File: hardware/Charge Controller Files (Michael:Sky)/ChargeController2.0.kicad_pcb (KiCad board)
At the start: 2 copper layers, 90.2 x 95.9 mm, 90 parts, among them J1 GND_TEST_01x01_Pin, J10 SOL_TEST_01x01_Pin, J13 Conn-1x2, J14 Conn-1x2, J15 Conn-1x2, J17 SCL_MAS_01x01_Pin, J18 SDA_MAS_01x01_Pin, J19 SYS-1x2, J2 SP_01x02_Pin, J3 BATT_TEST_01x01_Pin, J4 3.3V_PULLUP_01x02_Pin, J5 BATT_01x02_Pin, J6 Conn-1x2, J7 Conn-1x2, J8 Conn-1x2, J9 SYS_TEST_01x01_Pin, Q1 SI2318DS-T1-E3, Q10 SI2318DS-T1-E3, Q11 SI2318DS-T1-E3, Q12 SI2318DS-T1-E3, Q2 SI2318DS-T1-E3, Q3 SI2318DS-T1-E3, Q4 SI2318DS-T1-E3, Q5 AONS66614, Q6 AONS66614, Q7 AONS66614, Q8 AONS66614, Q9 SI2318DS-T1-E3, SW1 100SP1T1B1M1QEH, U1 BQ25756ERRVR

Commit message: PCB fixes
Routing changes
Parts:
- moved C17 1.58 mm to (199.0, 107.5)
- moved R_AC2 1.00 mm to (170.5, 105.5)
- moved D7 0.71 mm to (143.0, 51.7), turned to -90 degrees
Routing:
- net Net-(D7-PadC): track 27.7 -> 21.9 mm
- net Net-(Q1-DRAIN): track 56.0 -> 50.8 mm
- net Net-(Q11-DRAIN): track 119.2 -> 115.9 mm
- net /ACOV: track 14.3 -> 13.3 mm
- net /ACUV: track 15.8 -> 14.9 mm
- net GND: track 81.1 -> 80.5 mm

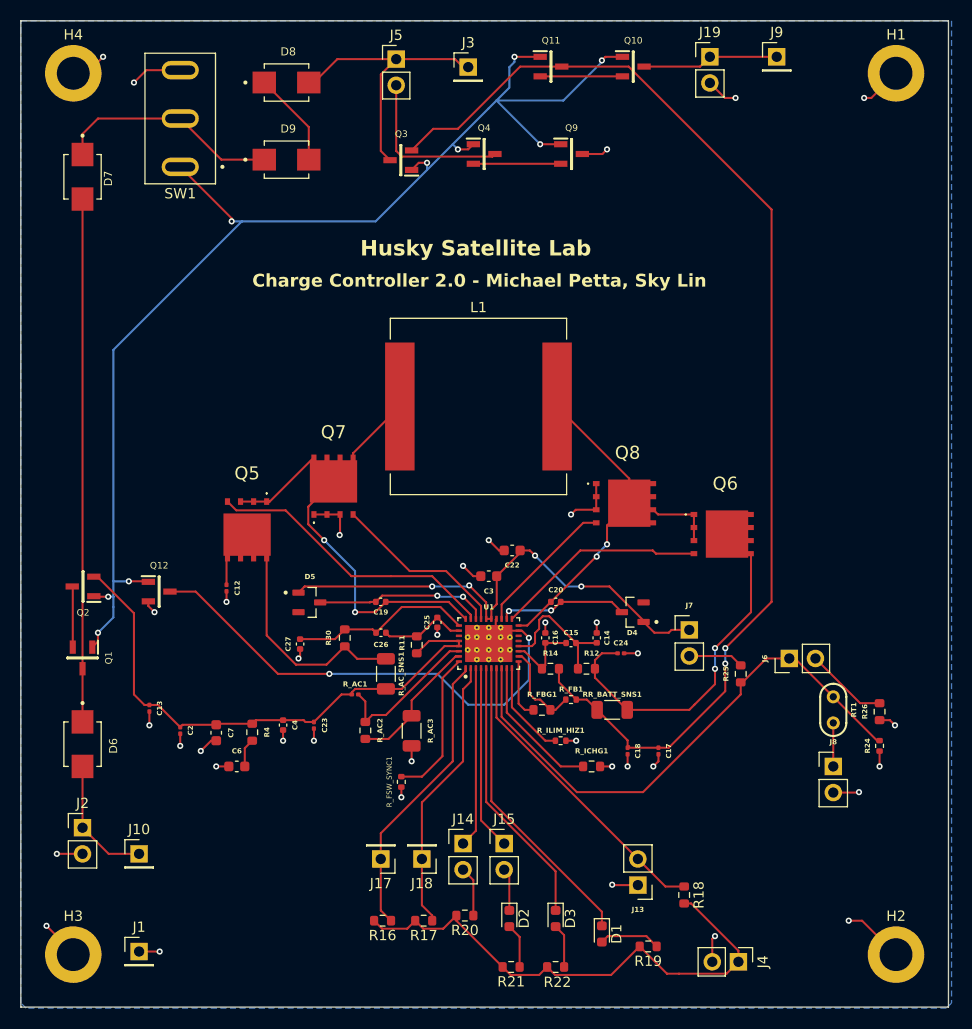
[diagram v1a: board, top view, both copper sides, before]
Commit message: PCB fixes
Changed RAC_3 symbol and footprint, changed Inhibits mosfets to later (better) version.
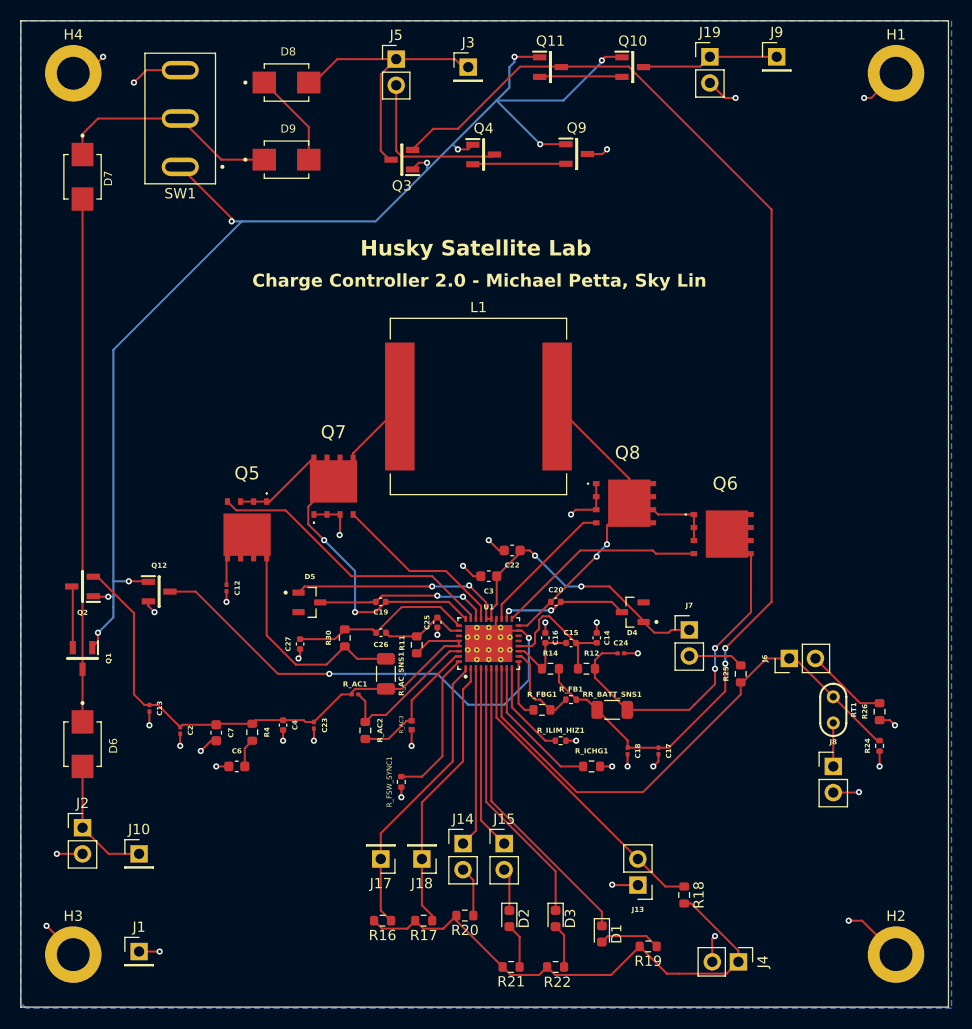
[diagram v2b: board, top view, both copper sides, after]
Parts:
- Q1, Q10, Q11, Q12, Q2, Q3, Q4, Q9: value SI2318DS-T1-E3 -> SI2318CDS-T1-GE3; footprint bmsfootprints:SI2318DS-T1-E3 -> bmsfootprints:SI2318CDS-T1-GE3
- R_AC3: value 53.25 -> RC0402FR-0753K6L; footprint Resistor_SMD:R_1206_3216Metric -> bmsfootprints:RC0402FR-0753K6L
- moved R_AC3 0.54 mm to (175.0, 105.0)
- moved Q9 0.50 mm to (191.1, 49.5)
- moved Q3 0.11 mm to (174.1, 50.0)
- moved Q10 0.07 mm to (196.5, 41.0)
- moved Q11 0.07 mm to (188.5, 41.0)
- moved Q4 0.07 mm to (182.0, 49.5)
- moved Q2 0.05 mm to (143.0, 91.5)
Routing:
- net PGND: track 50.2 -> 52.0 mm

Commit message: Ready for Manufacturing
Final push
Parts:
- removed D6: SS24, bmsfootprints:SS24
- removed Q12: SI2318CDS-T1-GE3, bmsfootprints:SI2318CDS-T1-GE3
- moved D7 6.84 mm to (143.0, 58.5)
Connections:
- D7 pad A: Net-(D6-PadC) -> Net-(J10-Pin_1)
- Q1 pad 3: Net-(D6-PadC) -> Net-(J10-Pin_1)
- Q10 pad 2: Net-(Q10-Pad2) -> Net-(J19-Pin_1)
- Q10 pad 3: Net-(J19-Pin_1) -> Net-(Q10-Pad3)
- Q11 pad 2: Net-(Q10-Pad2) -> Net-(Q10-Pad3)
- SW1 pad 1: /EN -> Net-(D7-PadC)
- SW1 pad 2: Net-(D7-PadC) -> /EN
- U1 pad 17: PGND -> GND
- U1 pad 22: PGND -> GND
- U1 pad 37: PGND -> GND
- U1 pad 38: PGND -> GND
- U1 pad 39: PGND -> GND
- U1 pad 40: PGND -> GND
- U1 pad 41: PGND -> GND
- U1 pad 42: PGND -> GND
- U1 pad 43: PGND -> GND
- U1 pad 44: PGND -> GND
- U1 pad 45: PGND -> GND
- U1 pad 46: PGND -> GND
- U1 pad 47: PGND -> GND
- U1 pad 48: PGND -> GND
- U1 pad 49: PGND -> GND
- U1 pad 50: PGND -> GND
- U1 pad 51: PGND -> GND
- U1 pad 52: PGND -> GND
- U1 pad 53: PGND -> GND
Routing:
- net PGND: track 52.0 -> 0.00 mm, vias 2 -> 0
- net Net-(D6-PadC): track 50.8 -> 0.00 mm
- net Net-(J10-Pin_1): track 12.5 -> 60.8 mm
- net Net-(Q10-Pad3): track 0.00 -> 10.5 mm
- net Net-(Q10-Pad2): track 8.00 -> 0.00 mm
- net GND: track 80.5 -> 86.7 mm
- net Net-(J19-Pin_1): track 13.3 -> 15.9 mm
- net /EN: track 126.0 -> 127.9 mm, vias 9 -> 10
- net Net-(C17-Pad1): track 115.9 -> 117.2 mm, vias 2 -> 4
- net Net-(D7-PadC): track 21.9 -> 20.8 mm
